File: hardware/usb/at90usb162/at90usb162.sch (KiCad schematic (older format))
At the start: 13 parts, among them IC1 AT90USB162-A, J1 USERPORT, P1 USB, SW1 DIPSW2, X1 8Mhz

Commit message: Hardware: Replaced dip-switch with simple pin header (use jumpers)
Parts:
- removed SW1: DIPSW2, ~, symbol DIPSW2
- added P2: RESET, symbol CONN_4
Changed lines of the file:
@@
 LIBS:valves
 LIBS:userport
-LIBS:dipswitch
 LIBS:at90usb162-cache
 EELAYER 27 0
@@
 Sheet 1 1
 Title "xlink usb adapter"
-Date "23 sep 2014"
+Date "28 jan 2015"
 Rev "1"
 Comp "Henning Bekel"
@@
 	5200 2100 5200 2150
 $Comp
-L DIPSW2 SW1
-U 1 1 54211D29
-P 5350 6300
-F 0 "SW1" H 5100 6650 60  0000 C CNN
-F 1 "DIPSW2" H 5450 6000 60  0000 C CNN
-F 2 "~" H 5300 6000 60  0000 C CNN
-F 3 "~" H 5300 6000 60  0000 C CNN
-	1    5350 6300
-	1    0    0    -1
-$EndComp
-$Comp
 L GND #PWR018
 U 1 1 54211D38
-P 5900 6400
-F 0 "#PWR018" H 5900 6400 30  0001 C CNN
-F 1 "GND" H 5900 6330 30  0001 C CNN
-F 2 "" H 5900 6400 60  0000 C CNN
-F 3 "" H 5900 6400 60  0000 C CNN
-	1    5900 6400
-	0    -1   -1   0
+P 5100 6300
+F 0 "#PWR018" H 5100 6300 30  0001 C CNN
+F 1 "GND" H 5100 6230 30  0001 C CNN
+F 2 "" H 5100 6300 60  0000 C CNN
+F 3 "" H 5100 6300 60  0000 C CNN
+	1    5100 6300
+	0    1    1    0
 $EndComp
 $Comp
 L GND #PWR019
 U 1 1 54211D45
-P 5900 6150
-F 0 "#PWR019" H 5900 6150 30  0001 C CNN
-F 1 "GND" H 5900 6080 30  0001 C CNN
-F 2 "" H 5900 6150 60  0000 C CNN
-F 3 "" H 5900 6150 60  0000 C CNN
-	1    5900 6150
-	0    -1   -1   0
-$EndComp
-Text Label 4700 6150 2    60   ~ 0
+P 5100 6200
+F 0 "#PWR019" H 5100 6200 30  0001 C CNN
+F 1 "GND" H 5100 6130 30  0001 C CNN
+F 2 "" H 5100 6200 60  0000 C CNN
+F 3 "" H 5100 6200 60  0000 C CNN
+	1    5100 6200
+	0    1    1    0
+$EndComp
+Text Label 5100 6400 2    60   ~ 0
 ATRESET
-Text Label 4700 6400 2    60   ~ 0
+Text Label 5100 6100 2    60   ~ 0
 D7
+$Comp
+L CONN_4 P2
+U 1 1 54C8BCC3
+P 5450 6250
+F 0 "P2" V 5400 6250 50  0000 C CNN
+F 1 "RESET" V 5500 6250 50  0000 C CNN
+F 2 "" H 5450 6250 60  0000 C CNN
+F 3 "" H 5450 6250 60  0000 C CNN
+	1    5450 6250
+	1    0    0    -1
+$EndComp
 $EndSCHEMATC

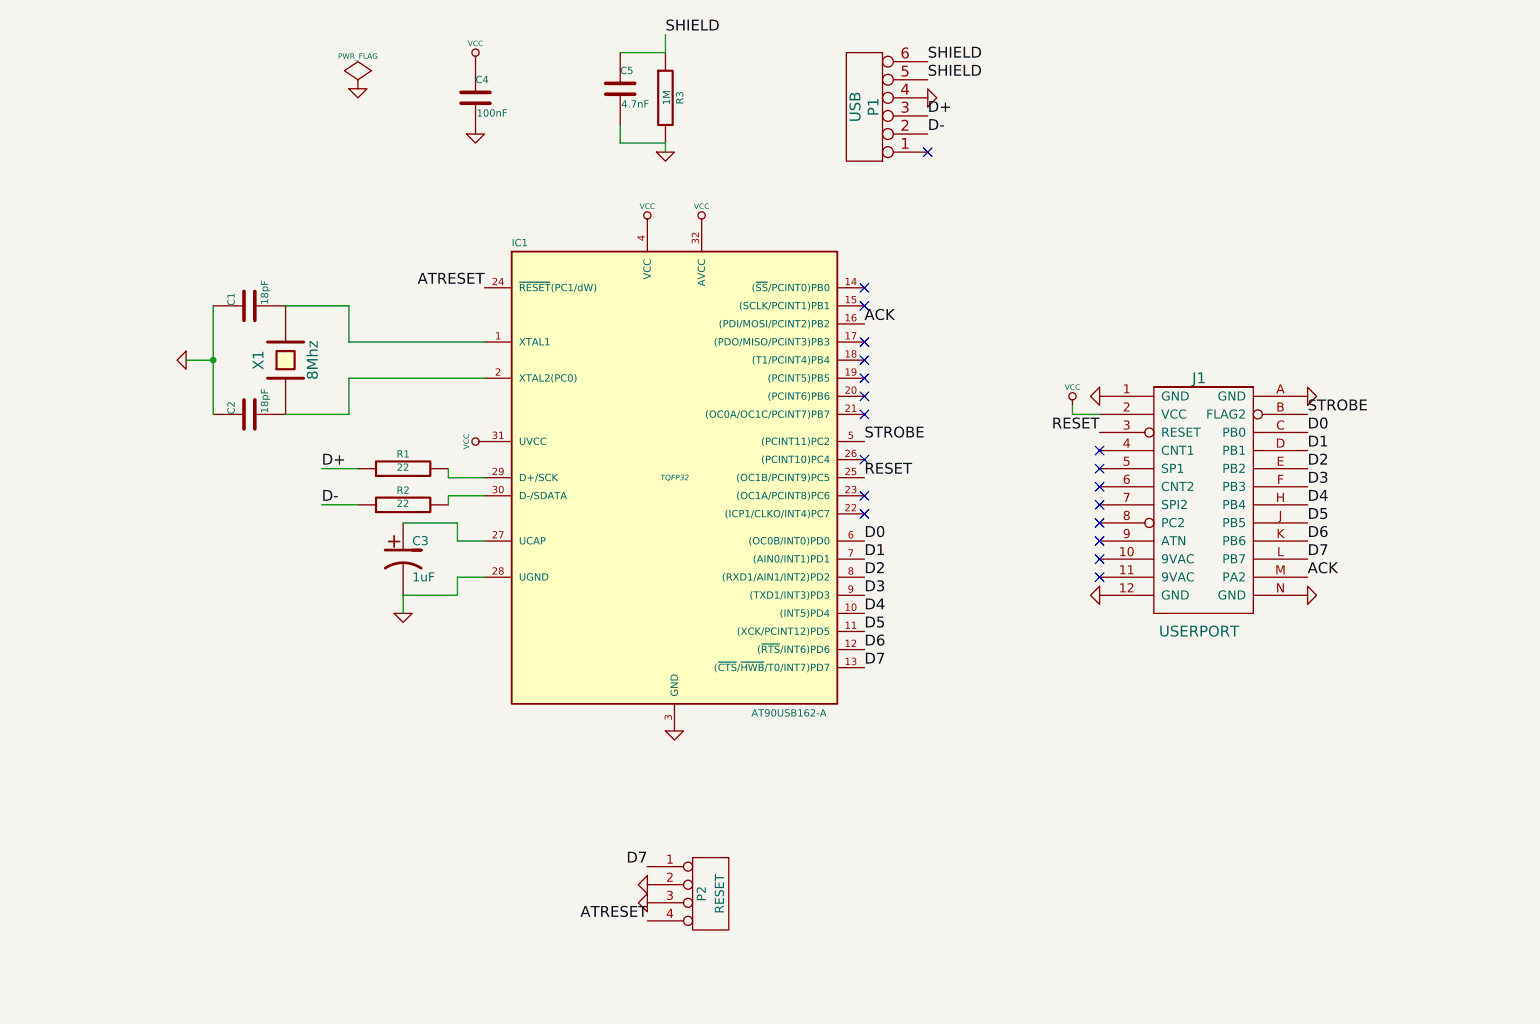
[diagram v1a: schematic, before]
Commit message: Hardware: Added current limiting resistors to data and handshake lines
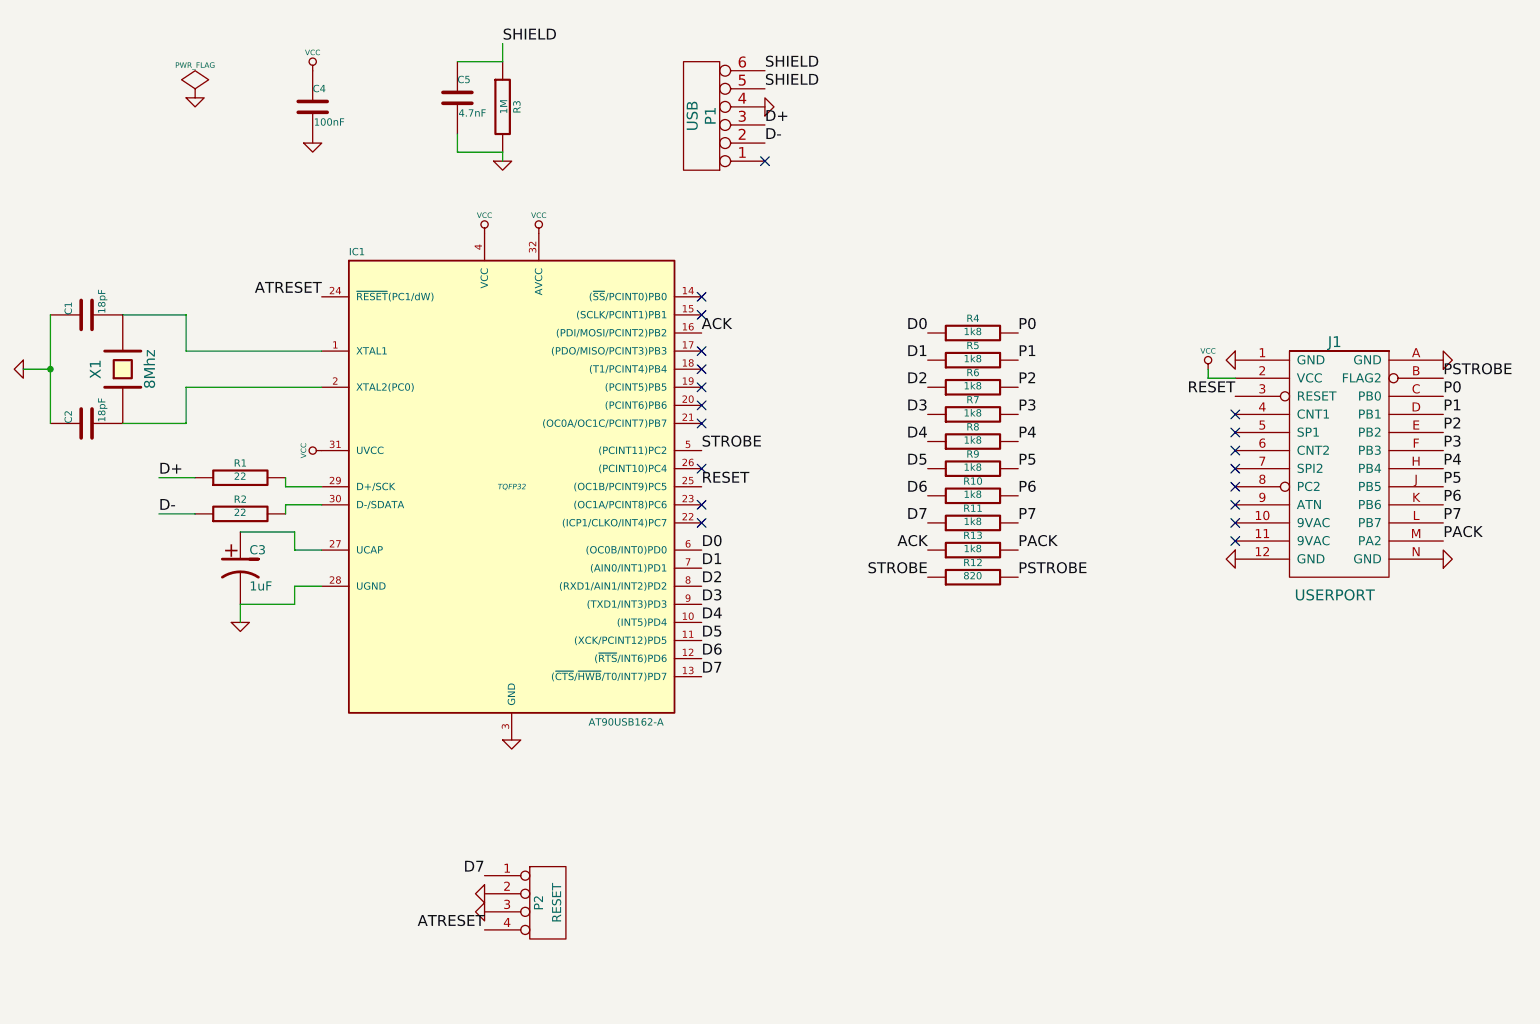
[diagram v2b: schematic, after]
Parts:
- added R10, R11, R13, R4, R5, R6, R7, R8, R9: 1k8, ~, symbol R
- added R12: 820, ~, symbol R
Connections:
- net ACK: now also R13.1; no longer J1.M (PA2)
- net D0: now also R4.1; no longer J1.C (PB0)
- net D1: now also R5.1; no longer J1.D (PB1)
- net D2: now also R6.1; no longer J1.E (PB2)
- net D3: now also R7.1; no longer J1.F (PB3)
- net D4: now also R8.1; no longer J1.H (PB4)
- net D5: now also R9.1; no longer J1.J (PB5)
- net D6: now also R10.1; no longer J1.K (PB6)
- net D7: now also R11.1; no longer J1.L (PB7)
- net STROBE: now also R12.1; no longer J1.B (FLAG2)
- new net P0: J1.C (PB0), R4.2
- new net P1: J1.D (PB1), R5.2
- new net P2: J1.E (PB2), R6.2
- new net P3: J1.F (PB3), R7.2
- new net P4: J1.H (PB4), R8.2
- new net P5: J1.J (PB5), R9.2
- new net P6: J1.K (PB6), R10.2
- new net P7: J1.L (PB7), R11.2
- new net PACK: J1.M (PA2), R13.2
- new net PSTROBE: J1.B (FLAG2), R12.2
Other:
- moved on the sheet: C1, C2, C3, C4, C5, IC1, J1, P1, P2, R1, R2, R3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

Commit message: Hardware: Added jumper to configure/adapt C64/C128 reset lines
On the C64 this jumper simply needs to be closed to allow resets. No copper
on the front layer around the pins to allow easy bridging.

On the C128, the reset signal at the userport only resets peripherals. The
jumper needs to be left open, and a wire must be run from the top pin to the
real reset line of the C128 to support hardware resets.
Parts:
- added JP1: JUMPER, ~, symbol JUMPER
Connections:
- net RESET: now also JP1.1; no longer J1.3 (RESET)
- new net EXTRES: J1.3 (RESET), JP1.2
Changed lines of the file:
@@
 Sheet 1 1
 Title "xlink usb adapter"
-Date "28 apr 2015"
+Date "3 jun 2015"
 Rev "2"
 Comp "Henning Bekel"
@@
 PACK
 Text Label 8350 3500 2    60   ~ 0
-RESET
+EXTRES
 NoConn ~ 8350 3700
 NoConn ~ 8350 3600
@@
 Text Label 9500 4200 0    60   ~ 0
 P7
+$Comp
+L JUMPER JP1
+U 1 1 556F07A0
+P 6350 5500
+F 0 "JP1" H 6350 5650 60  0000 C CNN
+F 1 "JUMPER" H 6350 5420 40  0000 C CNN
+F 2 "~" H 6350 5500 60  0000 C CNN
+F 3 "~" H 6350 5500 60  0000 C CNN
+	1    6350 5500
+	1    0    0    -1
+$EndComp
+Text Label 6050 5500 2    60   ~ 0
+RESET
+Text Label 6650 5500 0    60   ~ 0
+EXTRES
 $EndSCHEMATC
